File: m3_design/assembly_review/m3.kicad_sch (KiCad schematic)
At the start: 15 parts, among them J3 USB-C 2.0, U2 AP63203WU-7

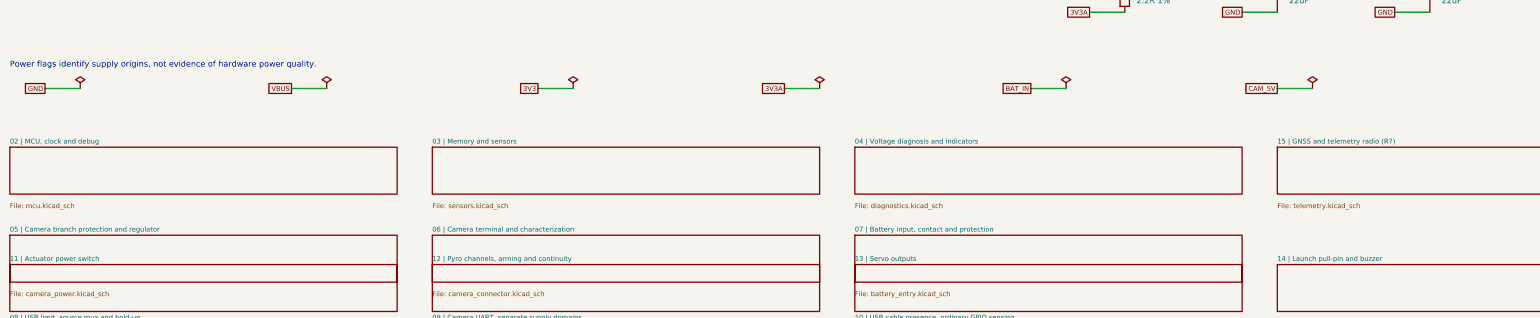
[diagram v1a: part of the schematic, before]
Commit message: R10: m3_design/r10_build.sh and per-family stage gate; m3_design/assembly_review rebuilt as M3-ASSY-R10 (board 883d2db5..., 46 x 90 mm); tools/check.sh passes at zero; binding note bound to the board
Co-Authored-By: Claude Opus 5.5 <noreply@anthropic.com>
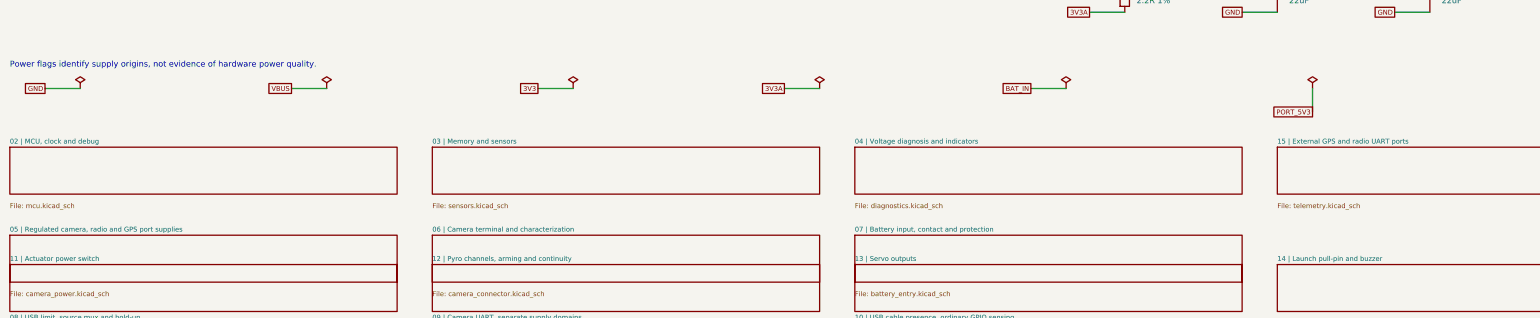
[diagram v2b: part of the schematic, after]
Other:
- sheet 05 | Camera branch protection and regulator renamed 05 | Regulated camera, radio and GPS port supplies
- sheet 15 | GNSS and telemetry radio (R7) renamed 15 | External GPS and radio UART ports
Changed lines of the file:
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@@
 		(title "01 | USB input and regulated supplies")
 		(date "2026-09-07")
-		(rev "M3-ASSY-R9")
+		(rev "M3-ASSY-R10")
 		(company "Single-board M3 candidate; full system incomplete"))
 	(text "01 | USB input and regulated supplies"
@@
 					(reference "#FLG06")
 					(unit 1)))))
-	(wire
-		(pts
-			(xy 302.26 218.44)
-			(xy 294.64 218.44))
-		(stroke
-			(width 0)
-			(type default))
-)
-	(global_label "CAM_5V"
-		(shape passive)
-		(at 294.64 218.44 0)
-		(effects
-			(font
-				(size 1.05 1.05))
-			(justify right))
-)
 	(sheet
 		(at 20.32 231.14)
@@
 		(fill
 			(color 0 0 0 0))
-		(property "Sheetname" "05 | Camera branch protection and regulator"
+		(property "Sheetname" "05 | Regulated camera, radio and GPS port supplies"
 			(at 20.32 248.92 0)
 			(effects
@@
 		(fill
 			(color 0 0 0 0))
-		(property "Sheetname" "15 | GNSS and telemetry radio (R7)"
+		(property "Sheetname" "15 | External GPS and radio UART ports"
 			(at 294.64 229.87 0)
 			(effects
@@
 				(path "/6007a7db-6a58-5660-8beb-956dea045ff8"
 					(page "15")))))
+	(wire
+		(pts
+			(xy 302.26 218.44)
+			(xy 302.26 223.52))
+		(stroke
+			(width 0)
+			(type default))
+)
+	(global_label "PORT_5V3"
+		(shape passive)
+		(at 302.26 223.52 0)
+		(effects
+			(font
+				(size 1.05 1.05))
+			(justify right))
+)
 	(sheet_instances
 		(path "/"

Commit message: R10 requirements-audit cuts and GAP fixes before review round 9
Implement adopted AUD-1 through AUD-10 and GAP-1 through GAP-5 after the single-switch pass.
Remove the advisory pull-pin, redundant probes and GPS/radio IO LDO cells; qualify the smaller
AONR21357 pair, correct C120 voltage rating, standardize shared-code capacitor lands, simplify
slow returns and fire-only copper, localize U9 output protection and add exactly two U401 VIPPO vias.
Record physical-current timing, coupled fire/source budget, C84 manual fitting and narrowed gate scopes.

Board SHA-256: 877d01996a59e9dd5c6dbc367274bb9a323a13982d67960fe46df9b0ee53205d
Board: 46 x 90 mm, 4 layers, 2365477 bytes; 225 footprints, 883 straight tracks, 323 vias.
Netlist SHA-256: 0843da709e2d7a757e9b35cdff48158a54012c5353619cbf409ab961efd2c3ca
Two fresh complete passing builds are byte-identical. Schematic: 700 pins; 22 seeded faults detected.

Final unskipped tools/check.sh: exit 0
DRC violations 0  unconnected 0  schematic parity 0  ERC 0
metadata / 3D model audit: OK
silkscreen outside the board outline: 0 stroke points
fit check: OK (CAD envelopes only)
R10 CAD contract (full): OK
routing hygiene: 0 failing, 0 allowlisted, 0 leftovers recorded
actuator safety contract: OK
Fab manifest: OK; 5 outputs match current CAD and export inputs
Self-tests: shell 4, fit 24, paste 5, routing 59, R10 131; three NumPy cases rerun and passed.

Fab: 215 CPL rows, 82 BOM codes; orientation / paste / manifest pass. Hot-plug: 2304 required
cases plus convergence and controls pass (simulation / Inference). Plate f1 280.9 Hz (Inference).
Live JLC: $84.43 vs $84.41 target, 46 Extended codes; R430 / U4 short. Procurement exit 1 is a
disclosed OQ-3 / ordering deviation, not a CAD gate pass. No quote accepted or order placed.
Firmware, bench, thermal/transient correlation, process acceptance, installed RF immunity and physical fit unverified.

This preparatory pass earns no clean-review credit. Start fresh full ten-lens round 9 on th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
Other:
- sheet 14 | Launch pull-pin and buzzer renamed 14 | Buzzer
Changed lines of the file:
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@@
 		(fill
 			(color 0 0 0 0))
-		(property "Sheetname" "14 | Launch pull-pin and buzzer"
+		(property "Sheetname" "14 | Buzzer"
 			(at 294.64 255.27 0)
 			(effects

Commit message: Finish R10 round 9 Minor fix pass
Complete the interrupted generator rebuild and apply the recorded round 9
Minor fixes: capacitor labels, cold-screen ordering, debugger instructions,
local route cleanups, gate fault detection and explicit R10 procurement limits.
Refresh the board-bound fabrication, supplier and validation records.

Round 9 reviewed 8bccb07: 0 Critical, 0 Major, 21 Minor groups. Round 10 will
freshly review this committed fix pass, including every changed CAD item.

Board SHA-256: b337fe63c258c85ba4120e75ad018afa0c22241f8bc21a4172787cf2887208d9
Board: 46 x 90 mm, 2366509 bytes. Two COMPLETE builds pass; all 21 generated
CAD and binding files are byte-identical.

Unskipped tools/check.sh: exit 0.
DRC violations 0; unconnected 0; schematic parity 0; ERC 0.
Metadata / 3D, silk, fit / plate, all 33 R10 rules, routing hygiene, actuator
contract and current 5-output fabrication manifest: OK.
Self-tests: shell 4, procurement 19, fit 24, paste 5, routing 59, R10 140;
3 NumPy cases rerun successfully, no unresolved skips. Hot-plug: 2304/2304
required cases pass (simulation / Inference).

Fab export, required fitting, orientation and paste pass: 215 CPL rows,
82 BOM codes. Fresh supplier/procurement checks correctly FAIL the known
$84.43 versus $84.41 cap and R430/U4 stock shortages; 46 Extended codes.
OQ-3 and final deviation acceptance remain pending. No firmware, bench,
installed RF immunity, physical fit, assembly-process or flight result claimed.

Evidence: docs/R10_VALIDATION.md and sources/r10_review/round9_fix_validation.json
and round9_fix_check.txt under m3_design/assembly_review. Native headless
KiCad environment uses the external D-R1-05 mouse-query workaround only;
repository gates and CAD rules are unchanged by that workaround.

Co-Authored-By: Claude Opus 5.5 <noreply@anthropic.com>
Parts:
- C10, C11, C6, C7, C8, C9: value 22uF -> 22uF 25V X5R 20%
- C28: value 4.7uF -> 4.7uF 16V X5R 10%
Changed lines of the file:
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@@
 					(size 1.27 1.27))
 				(justify left)))
-		(property "Value" "22uF"
+		(property "Value" "22uF 25V X5R 20%"
 			(at 281.94 115.57000000000001 0)
 			(effects
@@
 					(size 1.27 1.27))
 				(justify left)))
-		(property "Value" "22uF"
+		(property "Value" "22uF 25V X5R 20%"
 			(at 312.42 115.57000000000001 0)
 			(effects
@@
 					(size 1.27 1.27))
 				(justify left)))
-		(property "Value" "22uF"
+		(property "Value" "22uF 25V X5R 20%"
 			(at 297.18 156.20999999999998 0)
 			(effects
@@
 					(size 1.27 1.27))
 				(justify left)))
-		(property "Value" "22uF"
+		(property "Value" "22uF 25V X5R 20%"
 			(at 330.20000000000005 156.20999999999998 0)
 			(effects
@@
 					(size 1.27 1.27))
 				(justify left)))
-		(property "Value" "22uF"
+		(property "Value" "22uF 25V X5R 20%"
 			(at 297.18 199.39 0)
 			(effects
@@
 					(size 1.27 1.27))
 				(justify left)))
-		(property "Value" "22uF"
+		(property "Value" "22uF 25V X5R 20%"
 			(at 330.20000000000005 199.39 0)
 			(effects
@@
 					(size 1.27 1.27))
 				(justify left)))
-		(property "Value" "4.7uF"
+		(property "Value" "4.7uF 16V X5R 10%"
 			(at 66.04 146.04999999999998 0)
 			(effects
